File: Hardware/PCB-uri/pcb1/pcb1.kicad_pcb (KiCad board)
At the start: 2 copper layers, 5 parts, among them J1 Conn_01x04_Pin, U1 ATECC608B-SSHDA

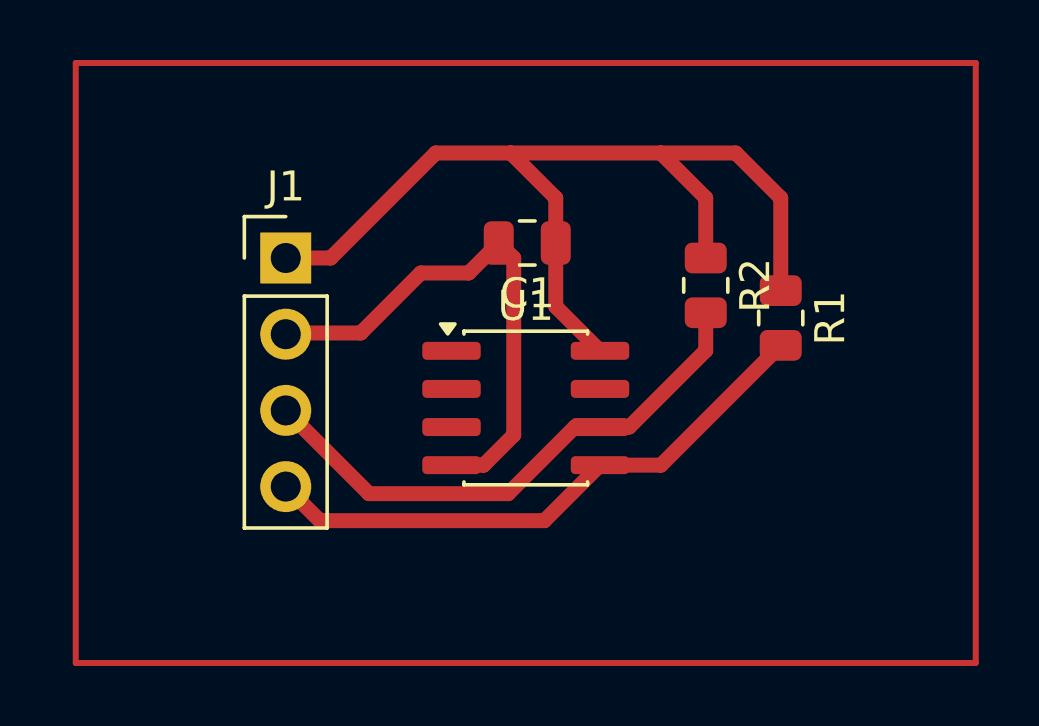
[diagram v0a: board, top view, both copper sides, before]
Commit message: Am mai lucrat la placa de retea sa intre intr-un dreptunghi de 100x75 si am mai lucrat putin la trasee (le-am facut de 0.5, ca sa stiu o treaba. Nu stiu cat de corect este, doar ca sunt constrans si de procedeul de gravare de acasa care este unul imperfect). Am dat comanda de piese, trebuie sa ajunga saptamana ce vine. Acum bag mare pe partea de software si ce am zis in mesajul anterior.
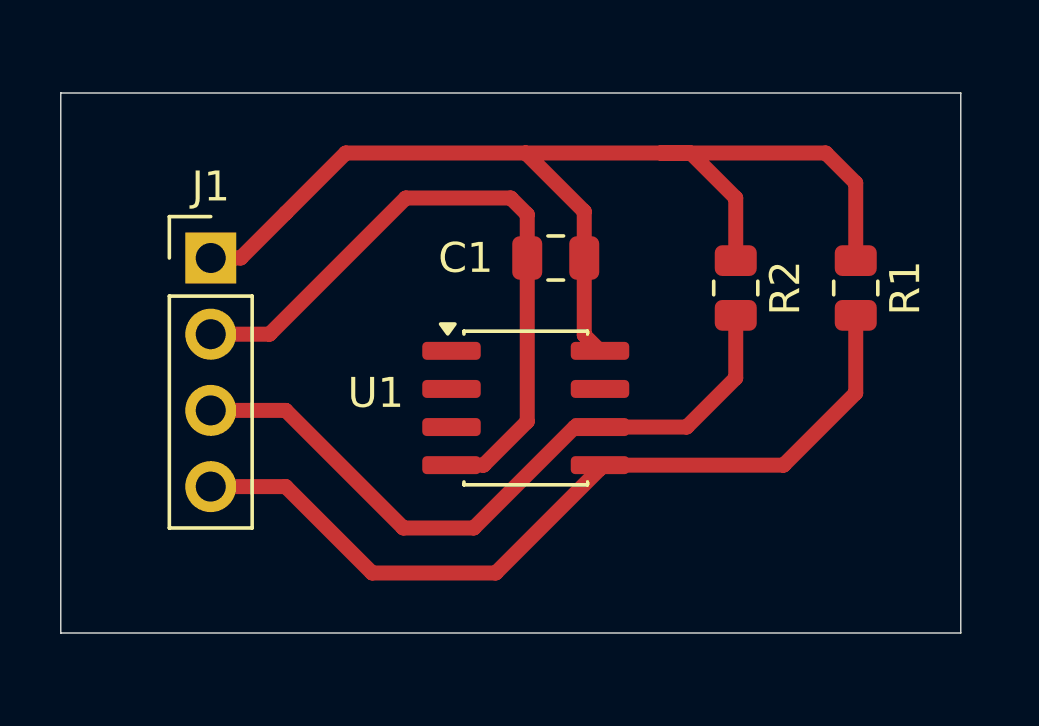
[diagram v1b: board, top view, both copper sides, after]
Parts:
- moved R1 2.69 mm to (61.0, 47.0)
- moved J1 2.50 mm to (39.5, 46.0)
- moved C1 1.07 mm to (51.0, 46.0)
- moved R2 1.00 mm to (57.0, 47.0)
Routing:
- net Net-(J1-Pin_4): track 19.4 -> 27.8 mm
- net GND: track 17.5 -> 22.7 mm
- net VCC: track 33.6 -> 38.8 mm
- net Net-(J1-Pin_3): track 18.4 -> 23.3 mm
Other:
- board outline added: 30 x 18 mm
